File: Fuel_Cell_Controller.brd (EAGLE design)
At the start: 203.2 x 163.8 mm, 137 parts, among them J1 BLUETOOTH, Q1 5.8A/30V/35mΩ, U1 MAX232PTH

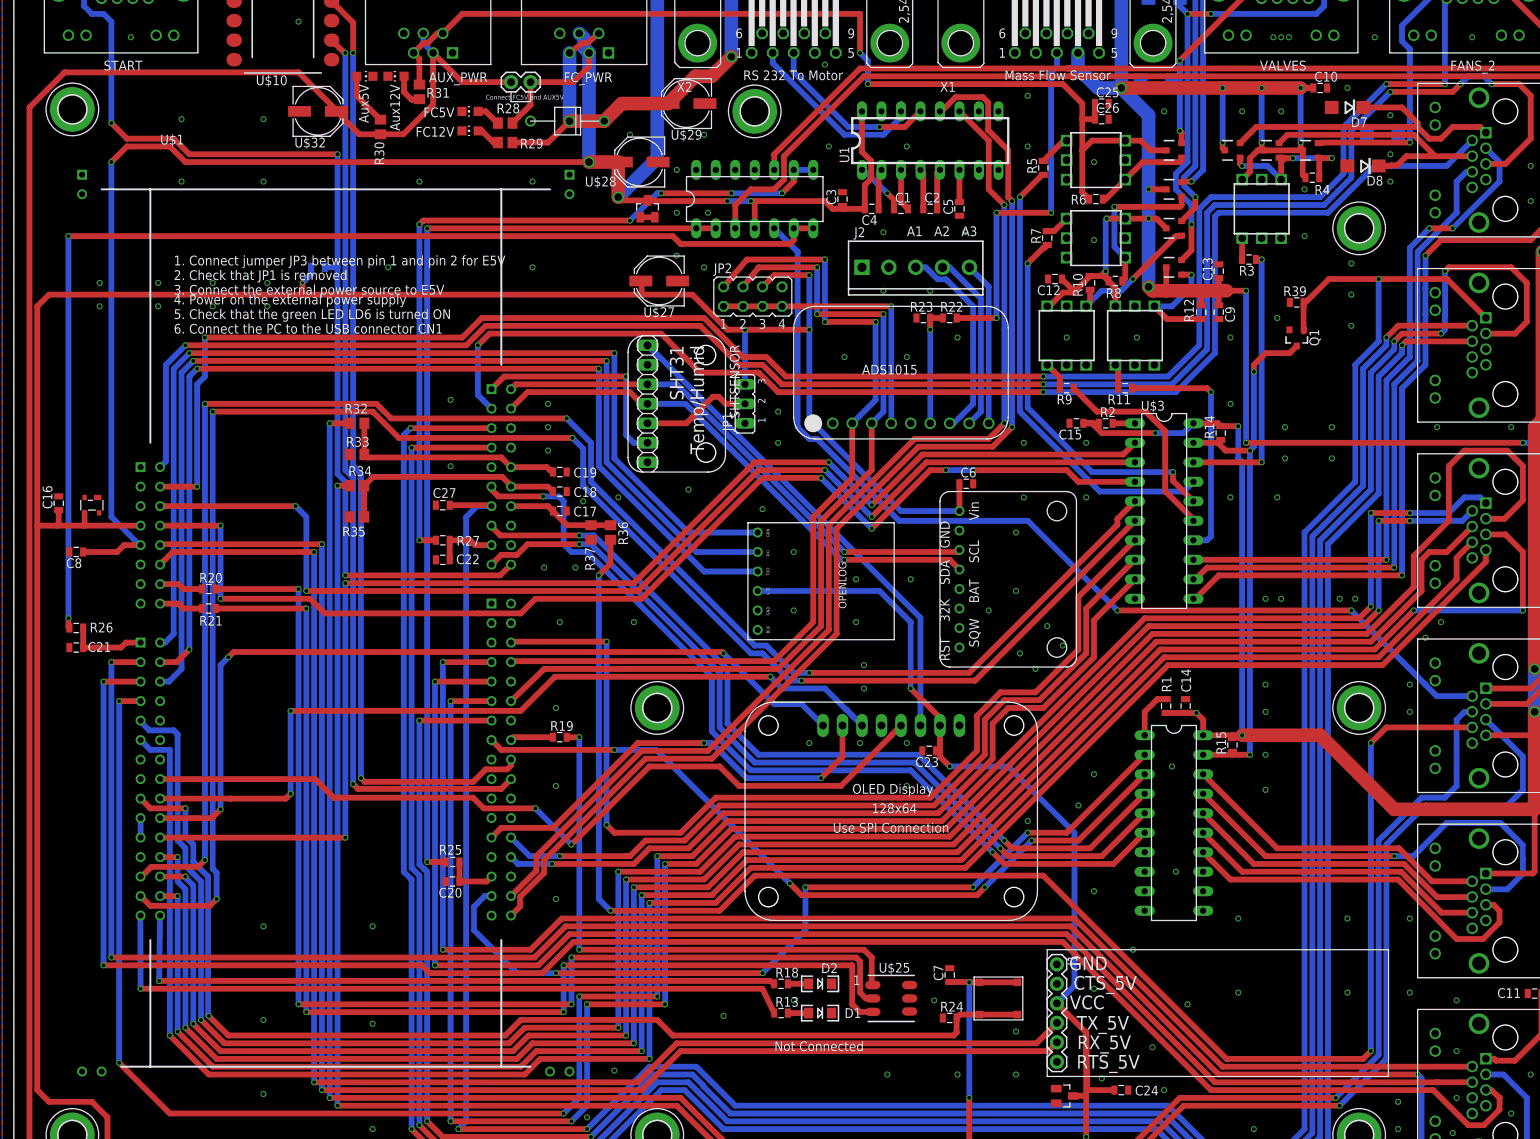
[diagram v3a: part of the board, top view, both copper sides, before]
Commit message: Adjusted how nucleo was powered and adding voltage dividers to pressure sensors
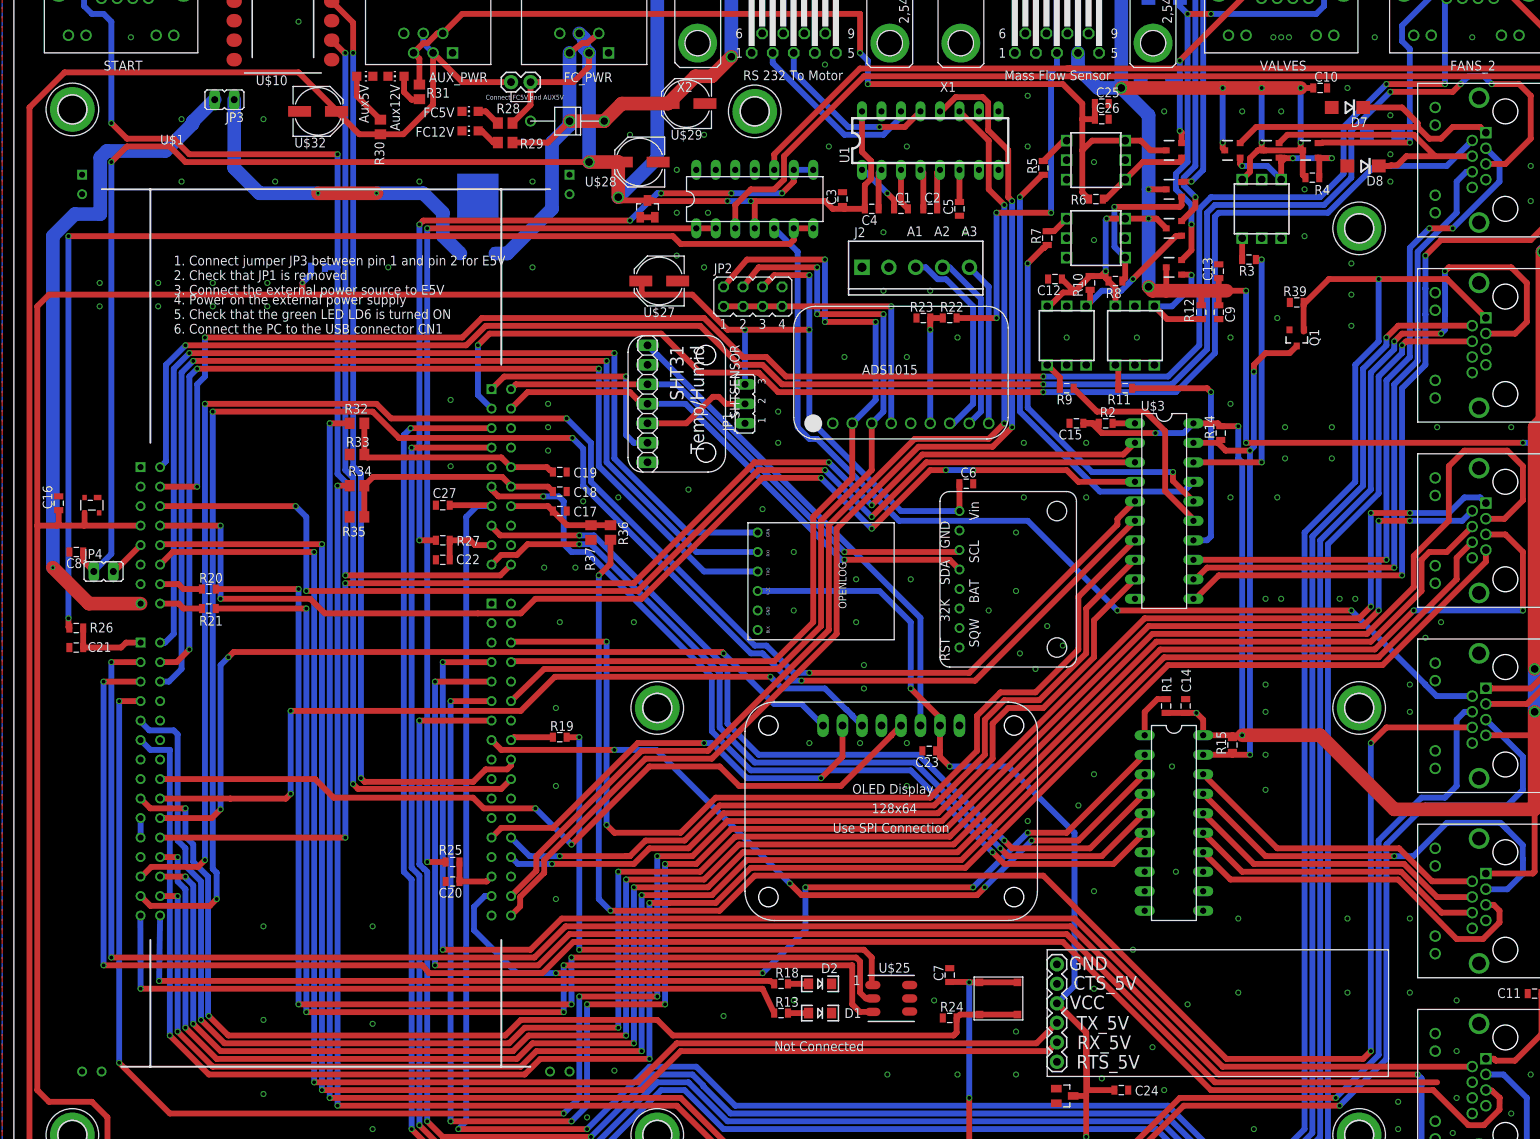
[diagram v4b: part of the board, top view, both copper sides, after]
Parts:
- added JP3, JP4: (no value), jumper:JP1
- added U$23: BA07CC0FP-E2, FCC_parts:TO252
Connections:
- new net N$1: JP4.2, U$1.5V
- new net N$31: JP3.1, U$23.2
- new net N$32: JP3.2, U$1.VIN
- new net _PRESSURE_1: PRESSURE.P$2
- new net _PRESSURE_2: PRESSURE.P$3
- new net _PRESSURE_3: PRESSURE.P$4
- new net _PRESSURE_4: PRESSURE.P$5
- net FC12V: now also U$23.1
- net FC5V: now also JP4.1; no longer U$1.5V
- net GND: now also U$23.3
- net PRESSURE_1: no longer PRESSURE.P$2
- net PRESSURE_2: no longer PRESSURE.P$3
- net PRESSURE_3: no longer PRESSURE.P$4
- net PRESSURE_4: no longer PRESSURE.P$5
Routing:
- net N$32: track 0.00 -> 89.5 mm, vias 0 -> 1
- net N$31: track 0.00 -> 44.8 mm, vias 0 -> 2
- net FC12V: track 430.3 -> 452.5 mm
- net N$1: track 0.00 -> 4.98 mm
- net PRESSURE_3: track 189.1 -> 184.6 mm
- net FC5V: track 622.2 -> 620.1 mm
- net PRESSURE_4: track 240.3 -> 239.6 mm
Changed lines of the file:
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@@
 </element>
 <element name="J1" library="FCC_parts" package="1X06BLUETOOTH" value="BLUETOOTH" x="179.07" y="30.48" smashed="yes" rot="R180">
-<attribute name="NAME" x="137.287" y="29.845" size="1.27" layer="25" font="vector" ratio="11" rot="R270"/>
 <attribute name="VALUE" x="132.842" y="29.845" size="1.27" layer="27" font="vector" ratio="11" rot="R270"/>
 </element>
@@
 <attribute name="NAME" x="165.354" y="115.6335" size="1.27" layer="25" font="vector" ratio="11"/>
 </element>
+<element name="JP4" library="jumper" library_urn="urn:adsk.eagle:library:252" package="JP1" package3d_urn="urn:adsk.eagle:package:15455/1" value="" x="11.684" y="79.756" rot="R270"/>
+<element name="U$23" library="FCC_parts" package="TO252" value="BA07CC0FP-E2" x="60.452" y="125.984" rot="MR0"/>
+<element name="JP3" library="jumper" library_urn="urn:adsk.eagle:library:252" package="JP1" package3d_urn="urn:adsk.eagle:package:15455/1" value="" x="27.432" y="141.224" rot="R90"/>
 </elements>
 <signals>
@@
 <via x="21.844" y="138.684" extent="1-16" drill="0.5"/>
 <via x="32.512" y="138.684" extent="1-16" drill="0.5"/>
-<via x="32.512" y="130.556" extent="1-16" drill="0.5"/>
+<via x="34.036" y="130.556" extent="1-16" drill="0.5"/>
 <via x="21.844" y="130.556" extent="1-16" drill="0.5"/>
 <via x="67.564" y="119.38" extent="1-16" drill="0.5"/>
@@
 <contactref element="R39" pad="1"/>
 <contactref element="Q1" pad="2"/>
+<contactref element="U$23" pad="3"/>
 </signal>
 <signal name="FROM_OPEN">
@@
 <via x="196.596" y="96.52" extent="1-16" drill="0.5"/>
 <wire x1="196.596" y1="96.52" x2="160.528" y2="96.52" width="0.762" layer="1"/>
-<wire x1="72.39" y1="147.32" x2="72.39" y2="138.43" width="1.778" layer="16"/>
+<wire x1="72.39" y1="138.43" x2="72.39" y2="147.32" width="1.778" layer="16"/>
 <wire x1="76.91" y1="138.43" x2="72.39" y2="138.43" width="1.778" layer="1"/>
 <via x="72.39" y="138.43" extent="1-16" drill="1"/>
@@
 <wire x1="138.6332" y1="145.3388" x2="141.224" y2="142.748" width="1.778" layer="16"/>
 <wire x1="141.224" y1="142.748" x2="144.272" y2="142.748" width="1.778" layer="16"/>
+<contactref element="U$23" pad="1"/>
+<wire x1="62.732" y1="121.184" x2="64.288" y2="121.184" width="1.778" layer="16"/>
+<wire x1="70.104" y1="127" x2="70.104" y2="135.636" width="1.778" layer="16"/>
+<wire x1="70.104" y1="135.636" x2="72.39" y2="137.922" width="1.778" layer="16"/>
+<wire x1="72.39" y1="137.922" x2="72.39" y2="138.43" width="1.778" layer="16"/>
+<wire x1="64.288" y1="121.184" x2="70.104" y2="127" width="1.778" layer="16"/>
 </signal>
 <signal name="N$3">
@@
 <signal name="PRESSURE_1">
 <contactref element="U$1" pad="PB_1"/>
-<contactref element="PRESSURE" pad="P$2"/>
-<wire x1="189.99" y1="15.26" x2="189.97" y2="15.24" width="0.762" layer="1"/>
 <wire x1="157.48" y1="15.24" x2="138.176" y2="34.544" width="0.762" layer="1"/>
 <wire x1="189.97" y1="15.24" x2="157.48" y2="15.24" width="0.762" layer="1"/>
@@
 <signal name="PRESSURE_3">
 <contactref element="U$1" pad="PC_2"/>
-<contactref element="PRESSURE" pad="P$4"/>
-<wire x1="189.99" y1="13.22" x2="185.42" y2="13.208" width="0.762" layer="1"/>
 <wire x1="185.42" y1="13.208" x2="156.464" y2="13.208" width="0.762" layer="1"/>
 <wire x1="156.464" y1="13.208" x2="137.16" y2="32.512" width="0.762" layer="1"/>
@@
 <signal name="PRESSURE_4">
 <contactref element="U$1" pad="PC_3"/>
-<contactref element="PRESSURE" pad="P$5"/>
 <wire x1="193.5654" y1="11.2012625" x2="193.548" y2="9.652" width="0.762" layer="1"/>
 <wire x1="192.532" y1="12.1076625" x2="193.5654" y2="11.2012625" width="0.762" layer="1"/>
@@
 <wire x1="54.102" y1="27.432" x2="53.213" y2="28.448" width="0.762" layer="1"/>
 <wire x1="53.213" y1="28.448" x2="11.684" y2="28.448" width="0.762" layer="1"/>
-<wire x1="191.77" y1="12.2" x2="192.4396625" y2="12.2" width="0.762" layer="1"/>
 <wire x1="192.4396625" y1="12.2" x2="192.532" y2="12.1076625" width="0.762" layer="1"/>
 </signal>
 <signal name="PRESSURE_2">
 <contactref element="U$1" pad="PC_0"/>
-<contactref element="PRESSURE" pad="P$3"/>
 <via x="182.88" y="14.224" extent="1-16" drill="0.5"/>
 <wire x1="156.972" y1="14.224" x2="182.88" y2="14.224" width="0.762" layer="1"/>
@@
 <via x="12.7" y="67.945" extent="1-16" drill="0.5"/>
 <wire x1="12.7" y1="67.945" x2="12.7" y2="29.464" width="0.762" layer="16"/>
-<wire x1="191.77" y1="14.24" x2="191.786" y2="14.224" width="0.762" layer="16"/>
 <wire x1="182.88" y1="14.224" x2="183.388" y2="13.716" width="0.762" layer="16"/>
 <wire x1="183.388" y1="13.716" x2="183.388" y2="5.08" width="0.762" layer="16"/>
@@
 <contactref element="RELAYBOARD2" pad="P$7"/>
 <contactref element="U$21" pad="C"/>
-<contactref element="U$1" pad="5V"/>
 <contactref element="U1" pad="16"/>
 <contactref element="C4" pad="2"/>
@@
 <wire x1="14.732" y1="135.128" x2="12.7" y2="133.096" width="0.762" layer="1"/>
 <via x="12.7" y="133.096" extent="1-16" drill="0.5"/>
-<wire x1="12.7" y1="133.096" x2="12.7" y2="86.868" width="0.762" layer="16"/>
-<wire x1="12.7" y1="86.868" x2="16.377284375" y2="83.190715625" width="0.762" layer="16"/>
-<wire x1="16.377284375" y1="83.190715625" x2="16.51" y2="83.190715625" width="0.762" layer="16"/>
-<wire x1="16.51" y1="83.190715625" x2="16.504284375" y2="83.185" width="0.762" layer="1"/>
-<wire x1="16.504284375" y1="83.185" x2="14.351" y2="83.185" width="0.762" layer="1"/>
-<wire x1="14.351" y1="83.185" x2="13.462" y2="82.296" width="0.762" layer="1"/>
-<wire x1="13.462" y1="82.296" x2="9.028" y2="82.296" width="0.762" layer="1"/>
 <via x="160.02" y="58.42" extent="1-16" drill="0.5"/>
 <wire x1="158.75" y1="58.42" x2="160.02" y2="58.42" width="0.762" layer="1"/>
@@
 <wire x1="148.717" y1="97.79" x2="152.4" y2="97.79" width="0.762" layer="16"/>
 <wire x1="152.4" y1="97.79" x2="153.67" y2="99.06" width="0.762" layer="16"/>
+<contactref element="JP4" pad="1"/>
+<wire x1="12.7" y1="82.042" x2="10.414" y2="79.756" width="0.762" layer="16"/>
+<wire x1="12.7" y1="133.096" x2="12.7" y2="82.042" width="0.762" layer="16"/>
+<wire x1="9.028" y1="82.296" x2="9.028" y2="81.142" width="0.762" layer="1"/>
+<wire x1="9.028" y1="81.142" x2="10.414" y2="79.756" width="0.762" layer="1"/>
 </signal>
 <signal name="FAN1_PWR">
@@
 <via x="197.612" y="14.224" extent="1-16" drill="0.5"/>
 </signal>
+<signal name="N$1">
+<contactref element="JP4" pad="2"/>
+<contactref element="U$1" pad="5V"/>
+<wire x1="12.954" y1="79.756" x2="13.075284375" y2="79.756" width="0.762" layer="1"/>
+<wire x1="13.075284375" y1="79.756" x2="16.51" y2="83.190715625" width="0.762" layer="1"/>
+</signal>
+<signal name="N$31">
+<contactref element="U$23" pad="2"/>
+<contactref element="JP3" pad="1"/>
+<wire x1="58.172" y1="121.184" x2="55.88" y2="123.476" width="1.778" layer="16"/>
+<wire x1="55.88" y1="123.476" x2="55.88" y2="126.492" width="1.778" layer="16"/>
+<wire x1="55.88" y1="126.492" x2="53.34" y2="129.032" width="1.778" layer="16"/>
+<wire x1="53.34" y1="129.032" x2="47.244" y2="129.032" width="1.778" layer="16"/>
+<via x="47.244" y="129.032" extent="1-16" drill="0.35"/>
+<via x="39.624" y="129.032" extent="1-16" drill="0.35"/>
+<wire x1="39.624" y1="129.032" x2="32.004" y2="129.032" width="1.778" layer="16"/>
+<wire x1="32.004" y1="129.032" x2="31.9238" y2="129.1122" width="1.778" layer="16"/>
+<wire x1="31.9238" y1="129.1122" x2="31.91395625" y2="129.1122" width="1.778" layer="16"/>
+<wire x1="31.91395625" y1="129.1122" x2="28.702" y2="132.32415625" width="1.778" layer="16"/>
+<wire x1="28.702" y1="132.32415625" x2="28.702" y2="141.224" width="1.778" layer="16"/>
+<wire x1="47.244" y1="129.032" x2="39.624" y2="129.032" width="1.778" layer="1"/>
+</signal>
+<signal name="N$32">
+<contactref element="JP3" pad="2"/>
+<contactref element="U$1" pad="VIN"/>
+<wire x1="26.162" y1="141.224" x2="23.2878" y2="138.3498" width="1.778" layer="16"/>
+<wire x1="23.2878" y1="138.3498" x2="23.2878" y2="138.08595625" width="1.778" layer="16"/>
+<wire x1="12.10195625" y1="134.5398" x2="11.2562" y2="133.69404375" width="1.778" layer="16"/>
+<wire x1="11.2562" y1="133.69404375" x2="11.2562" y2="126.3182" width="1.778" layer="16"/>
+<wire x1="11.2562" y1="126.3182" x2="7.94435625" y2="126.3182" width="1.778" layer="16"/>
+<wire x1="23.2878" y1="138.08595625" x2="19.74164375" y2="134.5398" width="1.778" layer="16"/>
+<wire x1="19.74164375" y1="134.5398" x2="12.10195625" y2="134.5398" width="1.778" layer="16"/>
+<wire x1="7.94435625" y1="126.3182" x2="5.08" y2="123.45384375" width="1.778" layer="16"/>
+<via x="5.08" y="80.264" extent="1-16" drill="0.35"/>
+<wire x1="5.08" y1="80.264" x2="9.773284375" y2="75.570715625" width="1.778" layer="1"/>
+<wire x1="9.773284375" y1="75.570715625" x2="16.51" y2="75.570715625" width="1.778" layer="1"/>
+<wire x1="5.08" y1="123.45384375" x2="5.08" y2="80.264" width="1.778" layer="16"/>
+</signal>
+<signal name="_PRESSURE_1">
+<contactref element="PRESSURE" pad="P$2"/>
+</signal>
+<signal name="_PRESSURE_2">
+<contactref element="PRESSURE" pad="P$3"/>
+</signal>
+<signal name="_PRESSURE_3">
+<contactref element="PRESSURE" pad="P$4"/>
+</signal>
+<signal name="_PRESSURE_4">
+<contactref element="PRESSURE" pad="P$5"/>
+</signal>
 </signals>

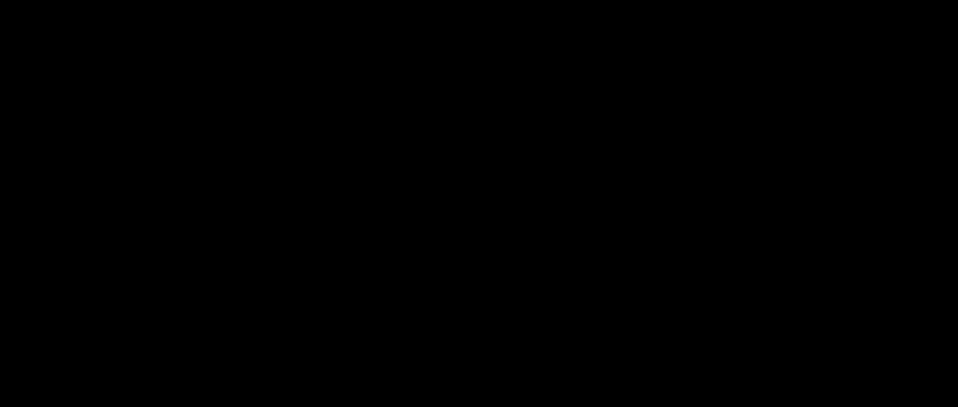
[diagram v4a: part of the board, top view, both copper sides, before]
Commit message: Added pressure sensor voltage dividers to schematic
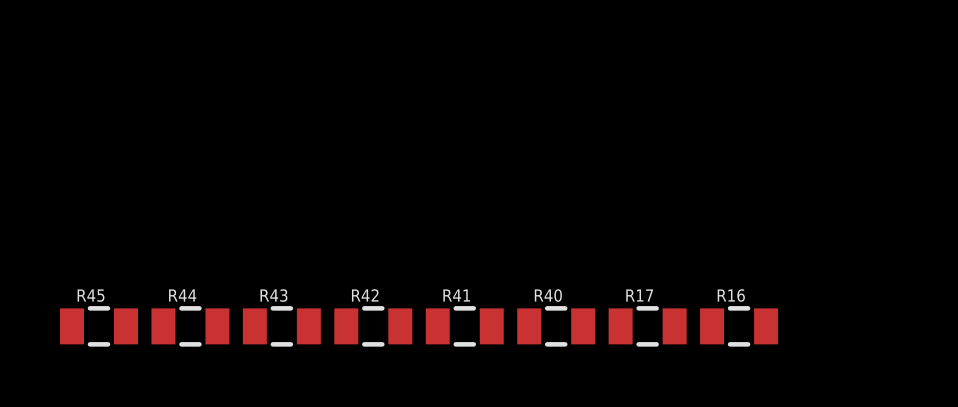
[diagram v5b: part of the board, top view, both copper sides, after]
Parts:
- added R16, R17, R40, R41, R42, R43, R44, R45: 10kΩ, SparkFun-Passives:0805
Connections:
- net GND: now also R17.1, R41.1, R43.1, R45.1
- net PRESSURE_1: now also R16.1, R17.2
- net PRESSURE_2: now also R40.1, R41.2
- net PRESSURE_3: now also R42.1, R43.2
- net PRESSURE_4: now also R44.1, R45.2
- net _PRESSURE_1: now also R16.2
- net _PRESSURE_2: now also R40.2
- net _PRESSURE_3: now also R42.2
- net _PRESSURE_4: now also R44.2
